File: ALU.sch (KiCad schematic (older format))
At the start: 10 parts, among them U1 74LS245, U10 74LS86, U2 74LS245, U3 74LS283, U4 74LS283, U5 74LS283, U6 74LS283, U7 74LS86, U8 74LS86, U9 74LS86

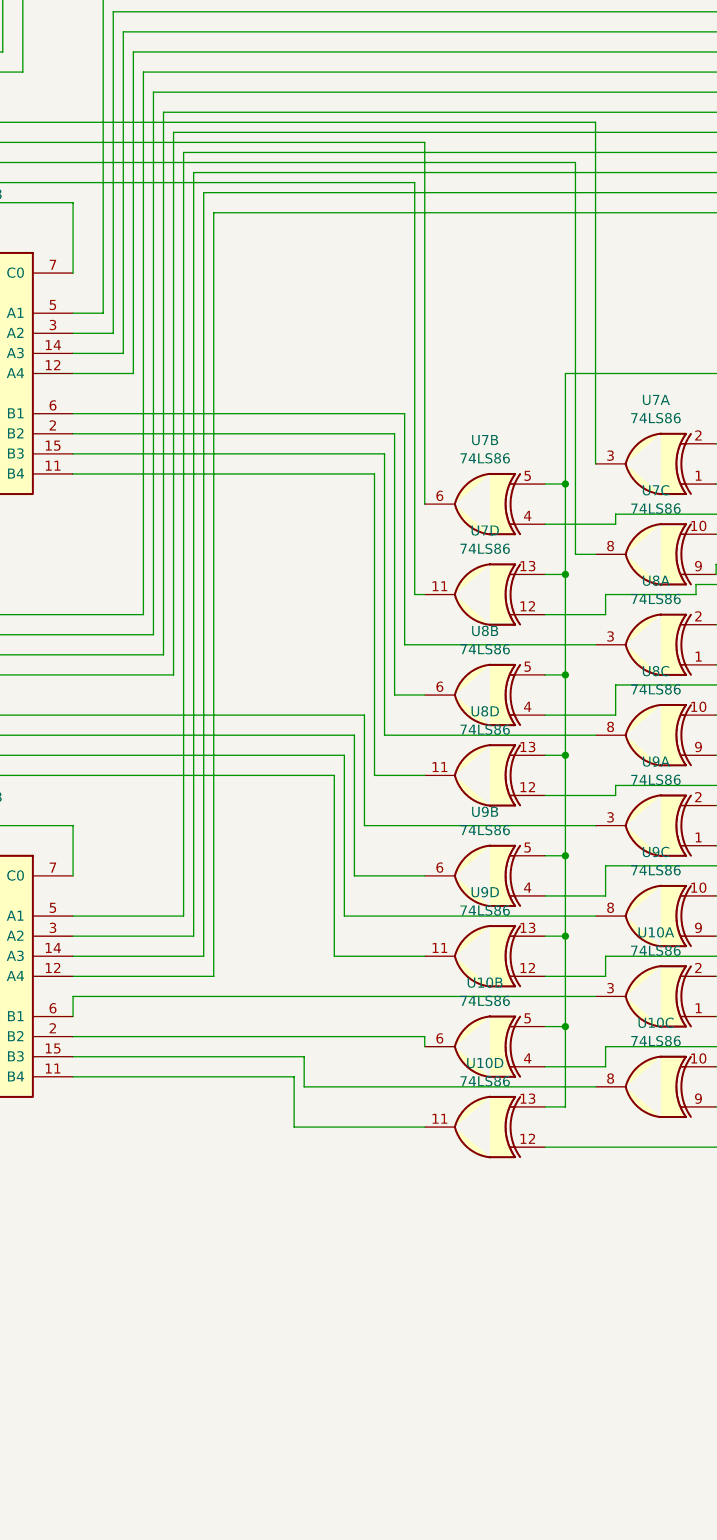
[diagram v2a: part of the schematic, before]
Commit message: Fixed power for multi part comps
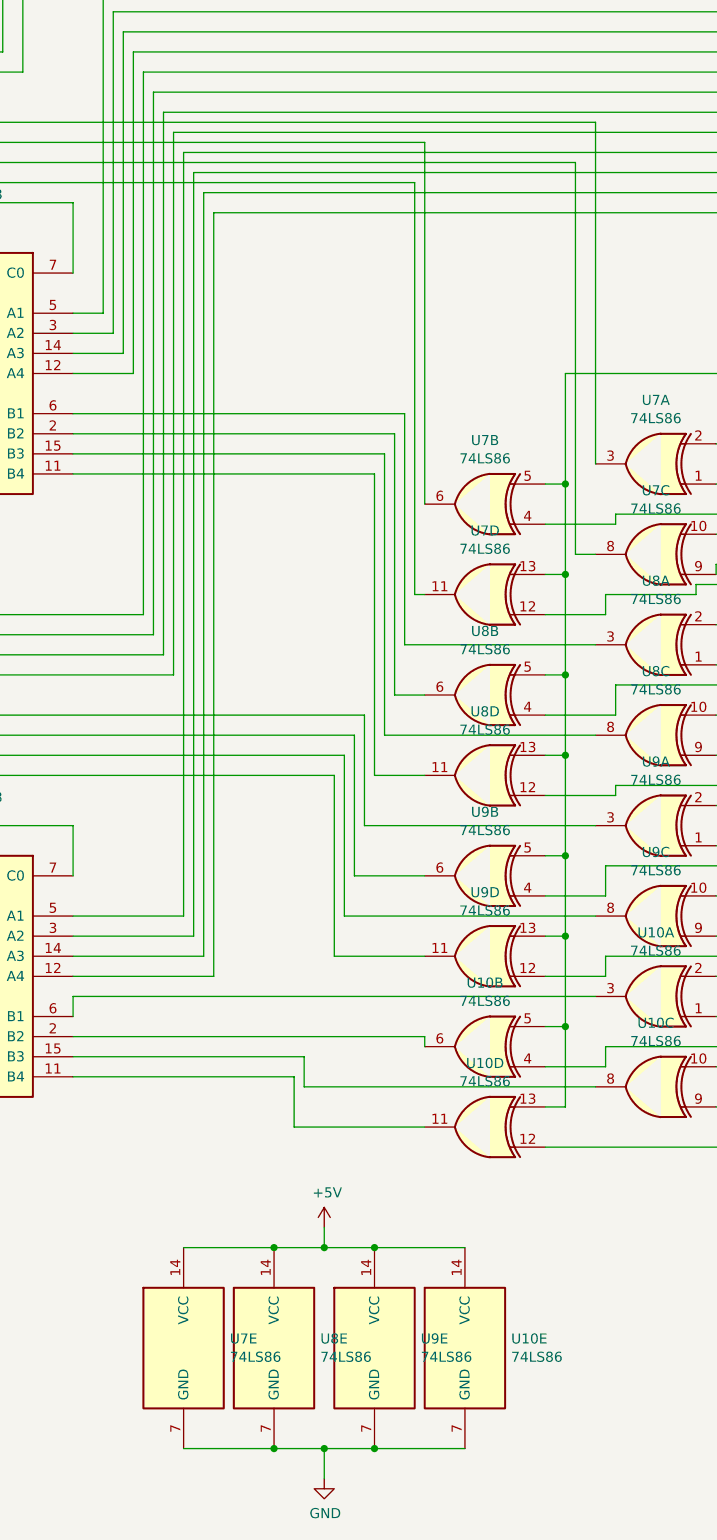
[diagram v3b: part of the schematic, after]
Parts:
- added unit 5 of U10
- added unit 5 of U7
- added unit 5 of U8
- added unit 5 of U9
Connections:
- net +5V: now also U10.14 (VCC), U7.14 (VCC), U8.14 (VCC), U9.14 (VCC)
- net GND: now also U10.7 (GND), U7.7 (GND), U8.7 (GND), U9.7 (GND)
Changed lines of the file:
@@
 Connection ~ 13350 6600
 Wire Wire Line
-	13350 6600 13350 7000
-Wire Wire Line
 	13250 7000 13350 7000
-Connection ~ 13350 7000
-Wire Wire Line
-	13350 7000 13350 7450
 Wire Wire Line
 	13250 7450 13350 7450
@@
 	10150 2900 10100 2900
 Wire Wire Line
-	12650 4850 12650 3050
-Wire Wire Line
 	12650 3050 10150 3050
 Wire Wire Line
@@
 	12200 6200 12200 7100
 Wire Wire Line
-	12200 7100 12650 7100
-Wire Wire Line
 	13500 7300 10900 7300
 Wire Wire Line
@@
 	12000 7950 12650 7950
 $Comp
-L power:+5V #PWR09
+L power:+5V #PWR013
 U 1 1 5F9C42E5
 P 9600 4900
-F 0 "#PWR09" H 9600 4750 50  0001 C CNN
+F 0 "#PWR013" H 9600 4750 50  0001 C CNN
 F 1 "+5V" H 9615 5073 50  0000 C CNN
 F 2 "" H 9600 4900 50  0001 C CNN
@@
 $EndComp
 $Comp
-L power:+5V #PWR013
+L power:+5V #PWR017
 U 1 1 5F9D4372
 P 10400 6400
-F 0 "#PWR013" H 10400 6250 50  0001 C CNN
+F 0 "#PWR017" H 10400 6250 50  0001 C CNN
 F 1 "+5V" H 10415 6573 50  0000 C CNN
 F 2 "" H 10400 6400 50  0001 C CNN
@@
 $EndComp
 $Comp
-L power:+5V #PWR011
+L power:+5V #PWR015
 U 1 1 5F9E19D2
 P 10400 3400
-F 0 "#PWR011" H 10400 3250 50  0001 C CNN
+F 0 "#PWR015" H 10400 3250 50  0001 C CNN
 F 1 "+5V" H 10415 3573 50  0000 C CNN
 F 2 "" H 10400 3400 50  0001 C CNN
@@
 $EndComp
 $Comp
-L power:+5V #PWR07
+L power:+5V #PWR011
 U 1 1 5F9EEF78
 P 9600 1900
-F 0 "#PWR07" H 9600 1750 50  0001 C CNN
+F 0 "#PWR011" H 9600 1750 50  0001 C CNN
 F 1 "+5V" H 9615 2073 50  0000 C CNN
 F 2 "" H 9600 1900 50  0001 C CNN
@@
 $EndComp
 $Comp
-L power:GND #PWR08
+L power:GND #PWR012
 U 1 1 5F9FCE79
 P 9600 3500
-F 0 "#PWR08" H 9600 3250 50  0001 C CNN
+F 0 "#PWR012" H 9600 3250 50  0001 C CNN
 F 1 "GND" H 9605 3327 50  0000 C CNN
 F 2 "" H 9600 3500 50  0001 C CNN
@@
 $EndComp
 $Comp
-L power:GND #PWR012
+L power:GND #PWR016
 U 1 1 5F9FD9D7
 P 10400 5000
-F 0 "#PWR012" H 10400 4750 50  0001 C CNN
+F 0 "#PWR016" H 10400 4750 50  0001 C CNN
 F 1 "GND" H 10405 4827 50  0000 C CNN
 F 2 "" H 10400 5000 50  0001 C CNN
@@
 $EndComp
 $Comp
-L power:GND #PWR010
+L power:GND #PWR014
 U 1 1 5FA0AF3B
 P 9600 6500
-F 0 "#PWR010" H 9600 6250 50  0001 C CNN
+F 0 "#PWR014" H 9600 6250 50  0001 C CNN
 F 1 "GND" H 9605 6327 50  0000 C CNN
 F 2 "" H 9600 6500 50  0001 C CNN
@@
 $EndComp
 $Comp
-L power:GND #PWR014
+L power:GND #PWR018
 U 1 1 5FA18552
 P 10400 8000
-F 0 "#PWR014" H 10400 7750 50  0001 C CNN
+F 0 "#PWR018" H 10400 7750 50  0001 C CNN
 F 1 "GND" H 10405 7827 50  0000 C CNN
 F 2 "" H 10400 8000 50  0001 C CNN
@@
 	7850 7000 7850 4850
 $Comp
-L power:+5V #PWR05
+L power:+5V #PWR09
 U 1 1 5FBCC769
 P 6700 3100
-F 0 "#PWR05" H 6700 2950 50  0001 C CNN
+F 0 "#PWR09" H 6700 2950 50  0001 C CNN
 F 1 "+5V" V 6715 3228 50  0000 L CNN
 F 2 "" H 6700 3100 50  0001 C CNN
@@
 $EndComp
 $Comp
-L power:+5V #PWR06
+L power:+5V #PWR010
 U 1 1 5FBCD4EB
 P 6700 5050
-F 0 "#PWR06" H 6700 4900 50  0001 C CNN
+F 0 "#PWR010" H 6700 4900 50  0001 C CNN
 F 1 "+5V" V 6715 5178 50  0000 L CNN
 F 2 "" H 6700 5050 50  0001 C CNN
@@
 	15100 4200 15500 4200
 $Comp
-L power:+5V #PWR01
+L power:+5V #PWR05
 U 1 1 6064A0D1
 P 6200 1900
-F 0 "#PWR01" H 6200 1750 50  0001 C CNN
+F 0 "#PWR05" H 6200 1750 50  0001 C CNN
 F 1 "+5V" H 6215 2073 50  0000 C CNN
 F 2 "" H 6200 1900 50  0001 C CNN
@@
 $EndComp
 $Comp
-L power:+5V #PWR03
+L power:+5V #PWR07
 U 1 1 60667C5F
 P 6200 3850
-F 0 "#PWR03" H 6200 3700 50  0001 C CNN
+F 0 "#PWR07" H 6200 3700 50  0001 C CNN
 F 1 "+5V" H 6215 4023 50  0000 C CNN
 F 2 "" H 6200 3850 50  0001 C CNN
@@
 $EndComp
 $Comp
-L power:GND #PWR02
+L power:GND #PWR06
 U 1 1 60685A34
 P 6200 3500
-F 0 "#PWR02" H 6200 3250 50  0001 C CNN
+F 0 "#PWR06" H 6200 3250 50  0001 C CNN
 F 1 "GND" H 6205 3327 50  0000 C CNN
 F 2 "" H 6200 3500 50  0001 C CNN
@@
 $EndComp
 $Comp
-L power:GND #PWR04
+L power:GND #PWR08
 U 1 1 606A37B5
 P 6200 5450
-F 0 "#PWR04" H 6200 5200 50  0001 C CNN
+F 0 "#PWR08" H 6200 5200 50  0001 C CNN
 F 1 "GND" H 6205 5277 50  0000 C CNN
 F 2 "" H 6200 5450 50  0001 C CNN
@@
 	-1   0    0    1
 $EndComp
+Wire Wire Line
+	13350 6600 13350 7000
+Connection ~ 13350 7000
+Wire Wire Line
+	13350 7000 13350 7450
+Wire Wire Line
+	12200 7100 12650 7100
+Wire Wire Line
+	12650 3050 12650 4850
+$Comp
+L 74xx:74LS86 U7
+U 5 1 60610FC5
+P 11450 9050
+F 0 "U7" H 11680 9096 50  0000 L CNN
+F 1 "74LS86" H 11680 9005 50  0000 L CNN
+F 2 "Package_DIP:DIP-14_W7.62mm" H 11450 9050 50  0001 C CNN
+F 3 "74xx/74ls86.pdf" H 11450 9050 50  0001 C CNN
+	5    11450 9050
+	1    0    0    -1
+$EndComp
+$Comp
+L 74xx:74LS86 U8
+U 5 1 60638886
+P 11900 9050
+F 0 "U8" H 12130 9096 50  0000 L CNN
+F 1 "74LS86" H 12130 9005 50  0000 L CNN
+F 2 "Package_DIP:DIP-14_W7.62mm" H 11900 9050 50  0001 C CNN
+F 3 "74xx/74ls86.pdf" H 11900 9050 50  0001 C CNN
+	5    11900 9050
+	1    0    0    -1
+$EndComp
+$Comp
+L 74xx:74LS86 U9
+U 5 1 6063A0D3
+P 12400 9050
+F 0 "U9" H 12630 9096 50  0000 L CNN
+F 1 "74LS86" H 12630 9005 50  0000 L CNN
+F 2 "Package_DIP:DIP-14_W7.62mm" H 12400 9050 50  0001 C CNN
+F 3 "74xx/74ls86.pdf" H 12400 9050 50  0001 C CNN
+	5    12400 9050
+	1    0    0    -1
+$EndComp
+$Comp
+L 74xx:74LS86 U10
+U 5 1 6063B891
+P 12850 9050
+F 0 "U10" H 13080 9096 50  0000 L CNN
+F 1 "74LS86" H 13080 9005 50  0000 L CNN
+F 2 "Package_DIP:DIP-14_W7.62mm" H 12850 9050 50  0001 C CNN
+F 3 "74xx/74ls86.pdf" H 12850 9050 50  0001 C CNN
+	5    12850 9050
+	1    0    0    -1
+$EndComp
+Wire Wire Line
+	11450 8550 11900 8550
+Wire Wire Line
+	12400 8550 12850 8550
+Wire Wire Line
+	11900 8550 12150 8550
+Connection ~ 11900 8550
+Connection ~ 12400 8550
+Wire Wire Line
+	11450 9550 11900 9550
+Connection ~ 11900 9550
+Wire Wire Line
+	11900 9550 12150 9550
+Connection ~ 12400 9550
+Wire Wire Line
+	12400 9550 12850 9550
+Wire Wire Line
+	12150 8550 12150 8450
+Connection ~ 12150 8550
+Wire Wire Line
+	12150 8550 12400 8550
+$Comp
+L power:+5V #PWR019
+U 1 1 6074679C
+P 12150 8450
+F 0 "#PWR019" H 12150 8300 50  0001 C CNN
+F 1 "+5V" H 12165 8623 50  0000 C CNN
+F 2 "" H 12150 8450 50  0001 C CNN
+F 3 "" H 12150 8450 50  0001 C CNN
+	1    12150 8450
+	1    0    0    -1
+$EndComp
+Wire Wire Line
+	12150 9550 12150 9700
+Connection ~ 12150 9550
+Wire Wire Line
+	12150 9550 12400 9550
+$Comp
+L power:GND #PWR020
+U 1 1 6076B36A
+P 12150 9700
+F 0 "#PWR020" H 12150 9450 50  0001 C CNN
+F 1 "GND" H 12155 9527 50  0000 C CNN
+F 2 "" H 12150 9700 50  0001 C CNN
+F 3 "" H 12150 9700 50  0001 C CNN
+	1    12150 9700
+	1    0    0    -1
+$EndComp
 $EndSCHEMATC

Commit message: Various Fixes
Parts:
- added U53: 74LS173, Package_DIP:DIP-16_W7.62mm, symbol 74xx:74LS173
- added U54, U55: 74HC02, Package_DIP:DIP-14_W7.62mm, symbol 74xx:74HC02
- added U56, U57: 74LS08, Package_DIP:DIP-14_W7.62mm, symbol 74xx:74LS08
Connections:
- net +5V: now also U54.14 (VCC), U55.14 (VCC), U56.14 (VCC), U57.14 (VCC)
- net GND: now also U53.1 (Oe1), U53.2 (Oe2), U54.7 (GND), U55.7 (GND), U56.7 (GND), U57.7 (GND)
- net at U1.3 (A1), U3.1 (S2): now also U54.2
- net at U1.5 (A3), U3.10 (S4): now also U54.5
- net at U1.4 (A2), U3.13 (S3): now also U54.6
- net at U1.2 (A0), U3.4 (S1): now also U54.3
- net at U1.7 (A5), U5.1 (S2): now also U54.8
- net at U1.9 (A7), U5.10 (S4): now also U54.11
- net at U1.8 (A6), U5.13 (S3): now also U54.12
- net at U1.6 (A4), U5.4 (S1): now also U54.9
- net at U2.7 (A5), U6.1 (S2): now also U55.8
- net at U2.9 (A7), U6.10 (S4): now also U55.11
- net at U2.8 (A6), U6.13 (S3): now also U55.12
- net at U2.6 (A4), U6.4 (S1): now also U55.9
- net at U6.9 (C4): now also U53.14 (D0)
- net at U2.3 (A1), U4.1 (S2): now also U55.2
- net at U2.5 (A3), U4.10 (S4): now also U55.5
- net at U2.4 (A2), U4.13 (S3): now also U55.6
- net at U2.2 (A0), U4.4 (S1): now also U55.3
- new net: U53.13 (D1), U56.8
- new net: U54.1, U57.2
- new net: U54.4, U57.1
- new net: U54.10, U57.5
- new net: U54.13, U57.4
- new net: U55.1, U57.10
- new net: U55.4, U57.9
- new net: U55.10, U56.13
- new net: U55.13, U56.12
- new net: U56.2, U57.3
- new net: U56.1, U57.6
- new net: U56.5, U57.8
- new net: U56.11, U56.4
- new net: U56.10, U56.3
- new net: U56.6, U56.9
- new net CF: U53.3 (Q0)
- new net CLK: U53.7 (Cp)
- new net CLR: U53.15 (Mr)
- new net ZF: U53.4 (Q1)
- new net ~FI: U53.10 (E2), U53.9 (E1)
- no-connect marks 0 -> 5

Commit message: Fixed ZIF
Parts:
- U1, U2: symbol 74xx:74LS245 -> 16bitCpu-rescue:74LS245-74xx
- U10, U7, U8, U9: symbol 74xx:74LS86 -> 16bitCpu-rescue:74LS86-74xx
- U3, U4, U5, U6: symbol 74xx:74LS283 -> 16bitCpu-rescue:74LS283-74xx
- U53: symbol 74xx:74LS173 -> 16bitCpu-rescue:74LS173-74xx
- U54, U55: symbol 74xx:74HC02 -> 16bitCpu-rescue:74HC02-74xx
- U56, U57: symbol 74xx:74LS08 -> 16bitCpu-rescue:74LS08-74xx

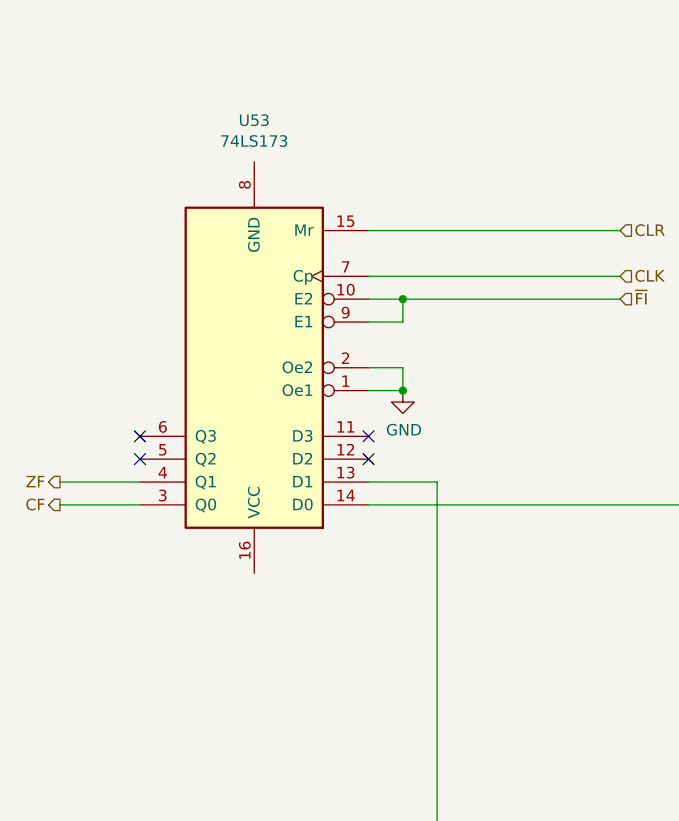
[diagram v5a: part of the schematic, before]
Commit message: Added GND and PWR in ALU and removed the Error
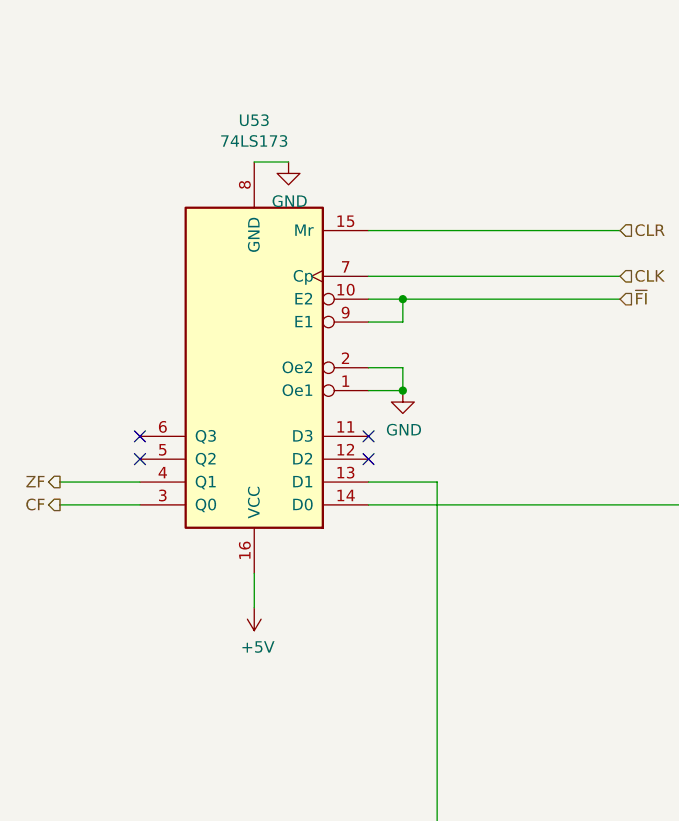
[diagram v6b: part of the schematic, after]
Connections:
- net +5V: now also U53.16 (VCC)
- net GND: now also U53.8 (GND)
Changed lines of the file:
@@
 NoConn ~ 1900 6900
 NoConn ~ 4350 6800
+Wire Wire Line
+	2400 5700 2550 5700
+Wire Wire Line
+	2400 7500 2400 7650
+$Comp
+L power:GND #PWR0171
+U 1 1 5F7E5CD0
+P 2550 5700
+F 0 "#PWR0171" H 2550 5450 50  0001 C CNN
+F 1 "GND" H 2555 5527 50  0000 C CNN
+F 2 "" H 2550 5700 50  0001 C CNN
+F 3 "" H 2550 5700 50  0001 C CNN
+	1    2550 5700
+	1    0    0    -1
+$EndComp
+$Comp
+L power:+5V #PWR0172
+U 1 1 5F826AFE
+P 2400 7650
+F 0 "#PWR0172" H 2400 7500 50  0001 C CNN
+F 1 "+5V" H 2415 7823 50  0000 C CNN
+F 2 "" H 2400 7650 50  0001 C CNN
+F 3 "" H 2400 7650 50  0001 C CNN
+	1    2400 7650
+	1    0    0    1
+$EndComp
 $EndSCHEMATC
